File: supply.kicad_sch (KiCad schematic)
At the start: 66 parts

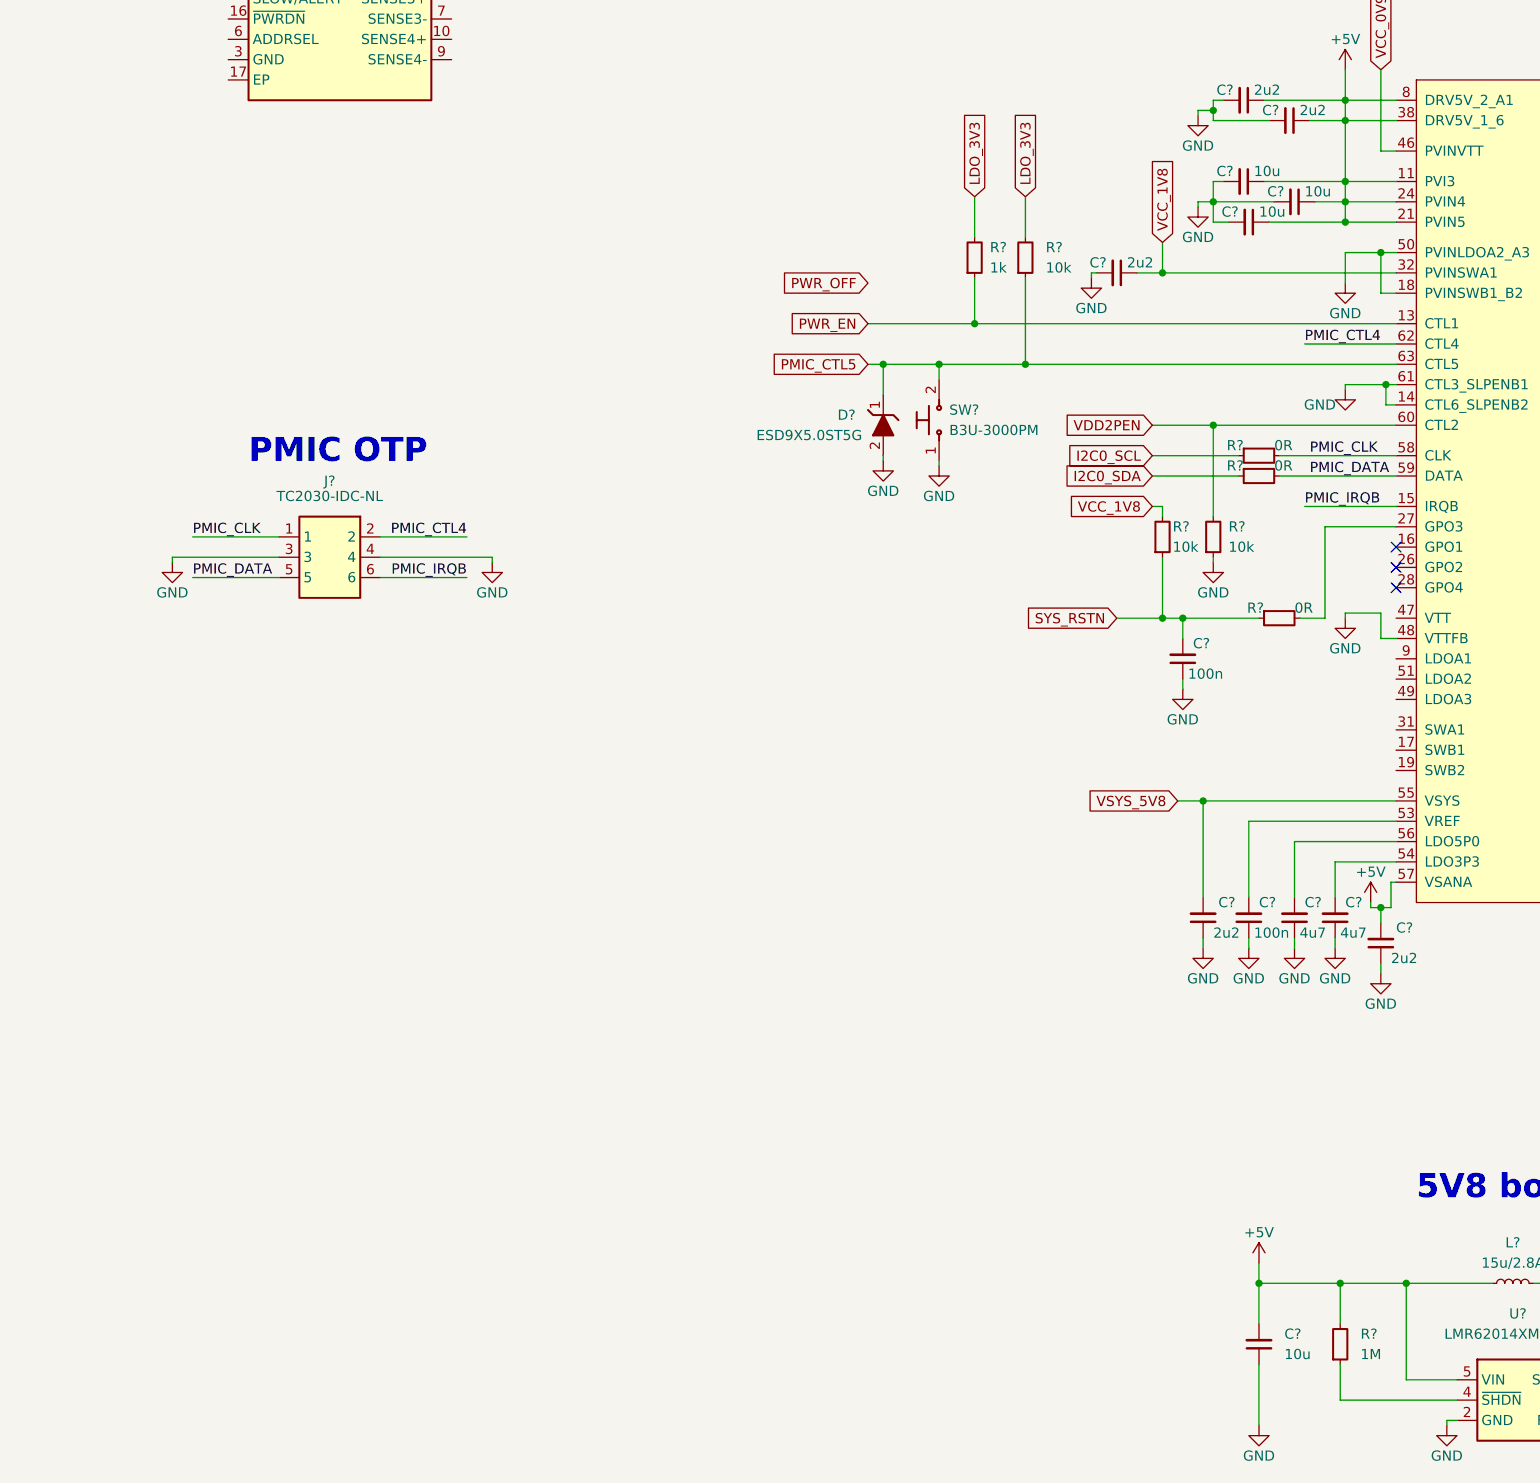
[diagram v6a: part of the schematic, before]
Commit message: [#52577] Add power mux for bank 1, 2 and 4 supply
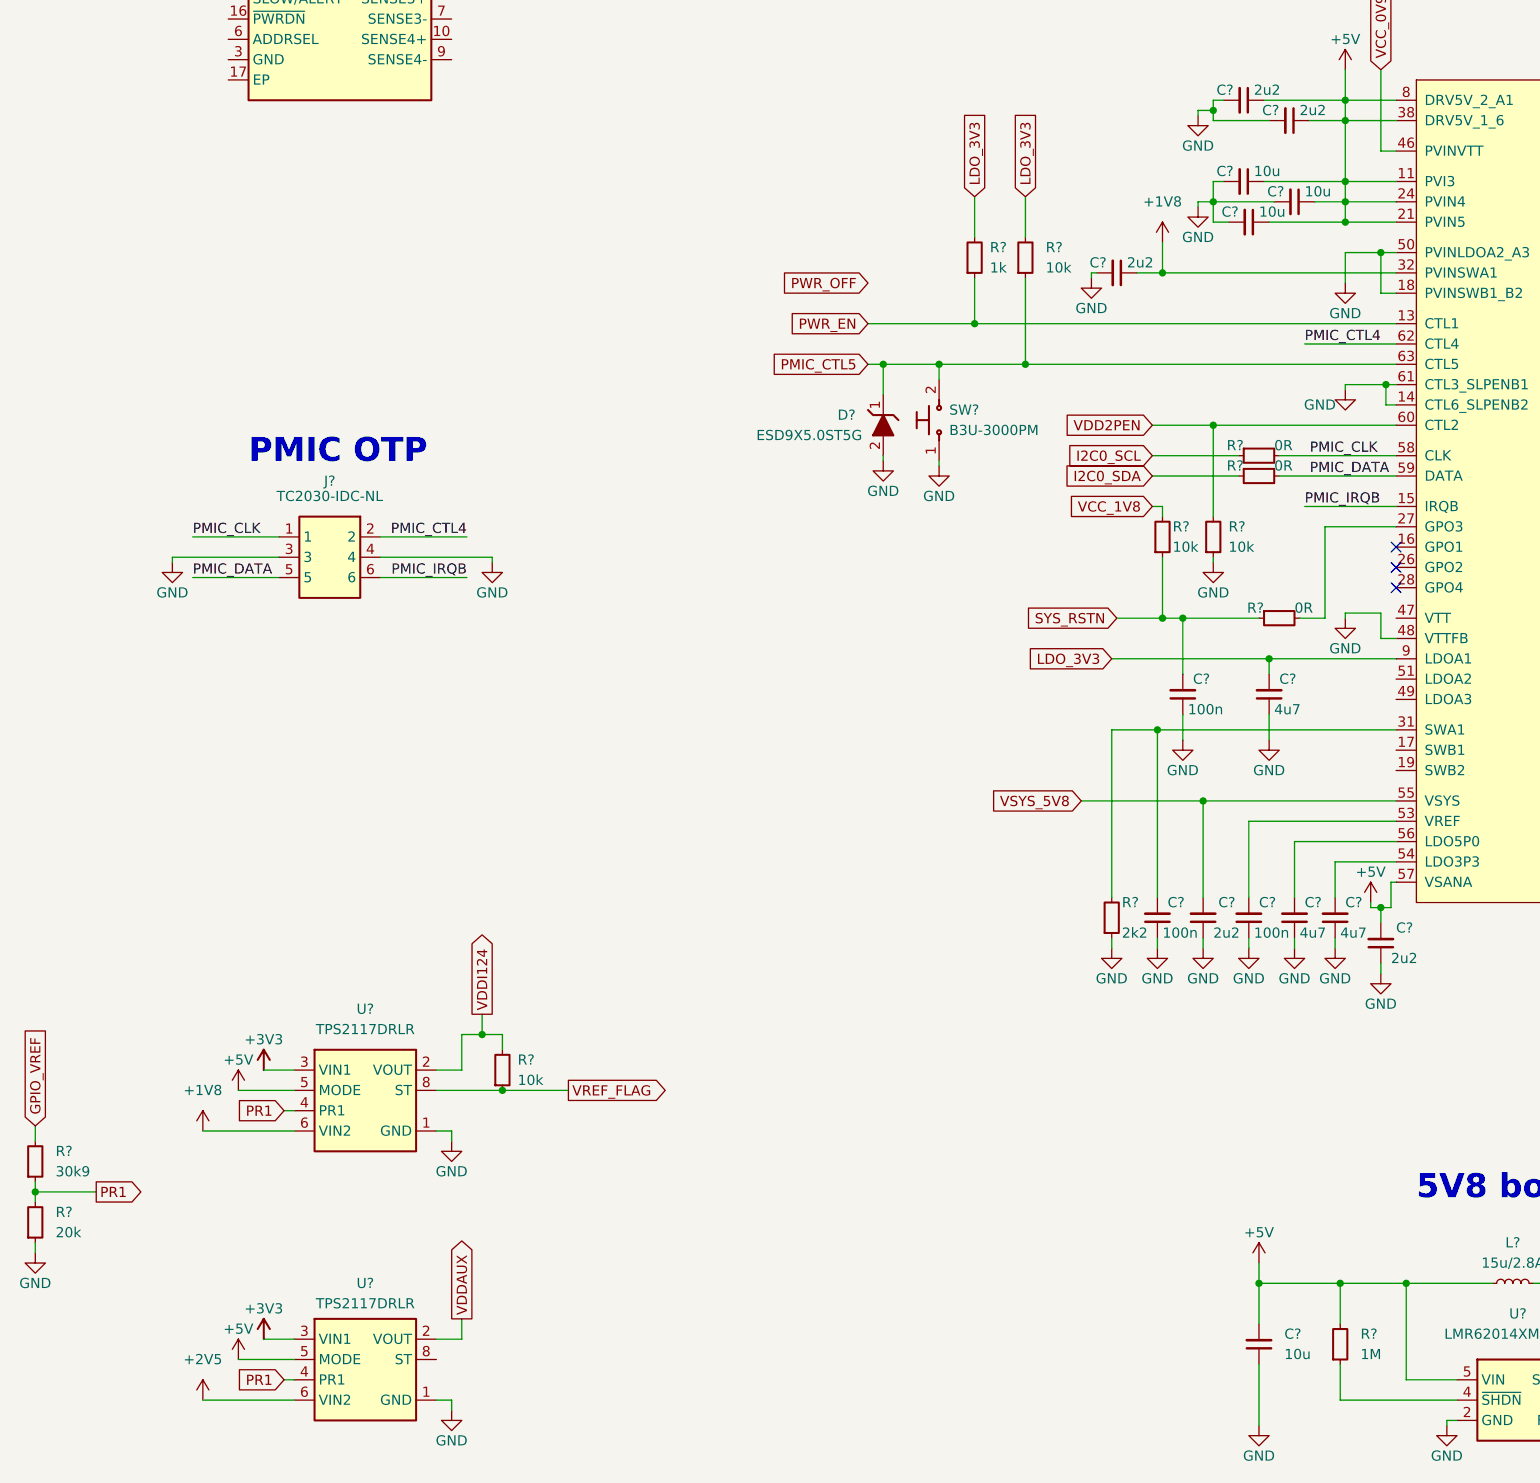
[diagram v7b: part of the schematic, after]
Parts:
- added C?: C_100n_0402, antmicro-footprints:C_0402_1005Metric, symbol antmicroCapacitors0402:C_100n_0402
- added C?: C_4u7_0402, antmicro-footprints:C_0402_1005Metric, symbol antmicroCapacitors0402:C_4u7_0402
- added R?: R_2k2_0402, antmicro-footprints:R_0402_1005Metric, symbol antmicroResistors0402:R_2k2_0402
- added R?: R_10k_0402, antmicro-footprints:R_0402_1005Metric, symbol antmicroResistors0402:R_10k_0402
- added R?: R_20k_0402, antmicro-footprints:R_0402_1005Metric, symbol antmicroResistors0402:R_20k_0402
- added R?: R_30k9_0402, antmicro-footprints:R_0402_1005Metric, symbol antmicroResistors0402:R_30k9_0402
- added U? (x2): TPS2117DRLR, antmicro-footprints:SOT-583, symbol antmicroPMICPowerDistributionSwitchesLoadDrivers:TPS2117DRLR
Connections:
- net +1V8: now also C?.1, U?.32 (PVINSWA1), U?.6 (VIN2)
- net +2V5: now also U?.6 (VIN2)
- net +3V3: now also U?.3 (VIN1), U?.3 (VIN1)
- net +5V: now also U?.5 (MODE), U?.5 (MODE)
- net GND: now also C?.1, C?.1, R?.1, R?.1, U?.1 (GND), U?.1 (GND)
- net LDO_3V3: now also U?.9 (LDOA1), C?.2
- net VCC_1V8: no longer C?.1, U?.32 (PVINSWA1)
- net at U?.31 (SWA1): now also C?.2, R?.2
- new net GPIO_VREF: R?.2
- new net PR1: R?.1, R?.2, U?.4 (PR1), U?.4 (PR1)
- new net VDDAUX: U?.2 (VOUT), U?.7 (VOUT)
- new net VDDI124: R?.2, U?.2 (VOUT), U?.7 (VOUT)
- new net VREF_FLAG: R?.1, U?.8 (ST)
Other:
- moved on the sheet: C?

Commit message: [#52577] Update PMIC's PVINVTT supply and GPO3 pullup
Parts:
- added R? (x2): R_0R_0402, antmicro-footprints:R_0402_1005Metric, symbol antmicroResistors0402:R_0R_0402
- U? (x3): Author (none) -> Antmicro; License (none) -> Apache-2.0
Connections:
- net VCC_0V9 is gone; now on net +1V15: U?.46 (PVINVTT)
- net VDDAUX: now also R?.2; no longer U?.2 (VOUT), U?.7 (VOUT)
- net VCC_1V8 renamed VDDI
- net VDDI: now also R?.2
- net VDDI124: no longer names the net of R?.2, U?.2 (VOUT), U?.7 (VOUT)
- net VDDI124: now also R?.1
- new net: R?.1, U?.2 (VOUT), U?.7 (VOUT)
- no-connect marks 5 -> 6
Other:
- note added: "GPIO Power Mux"
- moved on the sheet: C?, D?, L?, R?, SW?, U?
